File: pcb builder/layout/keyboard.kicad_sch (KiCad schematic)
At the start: 154 parts

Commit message: submoduling all folders KEKW
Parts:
- added U1: Elite-C, symbol keebio:Elite-C
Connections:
- net col0: now also U1.11 (8/PB4)
- net col1: now also U1.12 (9/PB5)
- net col10: now also U1.16 (15/PB1)
- net col11: now also U1.17 (A0/PF7)
- net col12: now also U1.18 (A1/PF6)
- net col13: now also U1.19 (A2/PF5)
- net col14: now also U1.20 (A3/PF4)
- net col2: now also U1.25 (B7)
- net col3: now also U1.26 (D5)
- net col4: now also U1.27 (C7)
- net col5: now also U1.28 (F1)
- net col6: now also U1.29 (F0)
- net col7: now also U1.13 (10/PB6)
- net col8: now also U1.14 (16/PB2)
- net col9: now also U1.15 (14/PB3)
- net row0: now also U1.5 (2/PD1)
- net row1: now also U1.6 (3/PD0)
- net row2: now also U1.7 (4/PD4)
- net row3: now also U1.8 (5/PC6)
- net row4: now also U1.9 (6/PD7)
- net row5: now also U1.10 (7/PE6)
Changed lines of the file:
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@@
+    )
+  )
+  (global_label "row1" (shape input) (at 427.99 54.61 180)
+    (effects (font (size 1.27 1.27)) (justify right))
+    (property "Intersheetrefs" "${INTERSHEET_REFS}" (at 427.99 54.61 0)
+      (effects (font (size 1.27 1.27)) hide)
+    )
+  )
+  (global_label "col4" (shape input) (at 445.77 80.01 270)
+    (effects (font (size 1.27 1.27)) (justify right))
+    (property "Intersheetrefs" "${INTERSHEET_REFS}" (at 445.77 80.01 0)
+      (effects (font (size 1.27 1.27)) hide)
+    )
+  )
+  (global_label "col8" (shape input) (at 463.55 67.31 0)
+    (effects (font (size 1.27 1.27)) (justify left))
+    (property "Intersheetrefs" "${INTERSHEET_REFS}" (at 463.55 67.31 0)
+      (effects (font (size 1.27 1.27)) hide)
     )
   )
@@
     )
   )
+  (global_label "row0" (shape input) (at 427.99 52.07 180)
+    (effects (font (size 1.27 1.27)) (justify right))
+    (property "Intersheetrefs" "${INTERSHEET_REFS}" (at 427.99 52.07 0)
+      (effects (font (size 1.27 1.27)) hide)
+    )
+  )
   (global_label "col13" (shape input) (at 375.92 16.51 180)
     (effects (font (size 1.27 1.27)) (justify right))
@@
     )
   )
+  (global_label "row5" (shape input) (at 427.99 64.77 180)
+    (effects (font (size 1.27 1.27)) (justify right))
+    (property "Intersheetrefs" "${INTERSHEET_REFS}" (at 427.99 64.77 0)
+      (effects (font (size 1.27 1.27)) hide)
+    )
+  )
   (global_label "col6" (shape input) (at 198.12 16.51 180)
     (effects (font (size 1.27 1.27)) (justify right))
@@
     )
   )
+  (global_label "row3" (shape input) (at 427.99 59.69 180)
+    (effects (font (size 1.27 1.27)) (justify right))
+    (property "Intersheetrefs" "${INTERSHEET_REFS}" (at 427.99 59.69 0)
+      (effects (font (size 1.27 1.27)) hide)
+    )
+  )
+  (global_label "col14" (shape input) (at 463.55 52.07 0)
+    (effects (font (size 1.27 1.27)) (justify left))
+    (property "Intersheetrefs" "${INTERSHEET_REFS}" (at 463.55 52.07 0)
+      (effects (font (size 1.27 1.27)) hide)
+    )
+  )
   (global_label "row1" (shape input) (at 22.86 60.96 180)
     (effects (font (size 1.27 1.27)) (justify right))
@@
     )
   )
+  (global_label "col2" (shape input) (at 440.69 80.01 270)
+    (effects (font (size 1.27 1.27)) (justify right))
+    (property "Intersheetrefs" "${INTERSHEET_REFS}" (at 440.69 80.01 0)
+      (effects (font (size 1.27 1.27)) hide)
+    )
+  )
+  (global_label "col5" (shape input) (at 448.31 80.01 270)
+    (effects (font (size 1.27 1.27)) (justify right))
+    (property "Intersheetrefs" "${INTERSHEET_REFS}" (at 448.31 80.01 0)
+      (effects (font (size 1.27 1.27)) hide)
+    )
+  )
   (global_label "col5" (shape input) (at 172.72 16.51 180)
     (effects (font (size 1.27 1.27)) (justify right))
@@
     )
   )
+  (global_label "col10" (shape input) (at 463.55 62.23 0)
+    (effects (font (size 1.27 1.27)) (justify left))
+    (property "Intersheetrefs" "${INTERSHEET_REFS}" (at 463.55 62.23 0)
+      (effects (font (size 1.27 1.27)) hide)
+    )
+  )
+  (global_label "col13" (shape input) (at 463.55 54.61 0)
+    (effects (font (size 1.27 1.27)) (justify left))
+    (property "Intersheetrefs" "${INTERSHEET_REFS}" (at 463.55 54.61 0)
+      (effects (font (size 1.27 1.27)) hide)
+    )
+  )
+  (global_label "col7" (shape input) (at 463.55 69.85 0)
+    (effects (font (size 1.27 1.27)) (justify left))
+    (property "Intersheetrefs" "${INTERSHEET_REFS}" (at 463.55 69.85 0)
+      (effects (font (size 1.27 1.27)) hide)
+    )
+  )
+  (global_label "col11" (shape input) (at 463.55 59.69 0)
+    (effects (font (size 1.27 1.27)) (justify left))
+    (property "Intersheetrefs" "${INTERSHEET_REFS}" (at 463.55 59.69 0)
+      (effects (font (size 1.27 1.27)) hide)
+    )
+  )
+  (global_label "col0" (shape input) (at 427.99 67.31 180)
+    (effects (font (size 1.27 1.27)) (justify right))
+    (property "Intersheetrefs" "${INTERSHEET_REFS}" (at 427.99 67.31 0)
+      (effects (font (size 1.27 1.27)) hide)
+    )
+  )
+  (global_label "row2" (shape input) (at 427.99 57.15 180)
+    (effects (font (size 1.27 1.27)) (justify right))
+    (property "Intersheetrefs" "${INTERSHEET_REFS}" (at 427.99 57.15 0)
+      (effects (font (size 1.27 1.27)) hide)
+    )
+  )
   (global_label "col14" (shape input) (at 401.32 16.51 180)
     (effects (font (size 1.27 1.27)) (justify right))
@@
     )
   )
+  (global_label "row4" (shape input) (at 427.99 62.23 180)
+    (effects (font (size 1.27 1.27)) (justify right))
+    (property "Intersheetrefs" "${INTERSHEET_REFS}" (at 427.99 62.23 0)
+      (effects (font (size 1.27 1.27)) hide)
+    )
+  )
   (global_label "row5" (shape input) (at 22.86 162.56 180)
     (effects (font (size 1.27 1.27)) (justify right))
@@
     )
   )
+  (global_label "col9" (shape input) (at 463.55 64.77 0)
+    (effects (font (size 1.27 1.27)) (justify left))
+    (property "Intersheetrefs" "${INTERSHEET_REFS}" (at 463.55 64.77 0)
+      (effects (font (size 1.27 1.27)) hide)
+    )
+  )
   (global_label "col7" (shape input) (at 223.52 16.51 180)
     (effects (font (size 1.27 1.27)) (justify right))
@@
     )
   )
+  (global_label "col3" (shape input) (at 443.23 80.01 270)
+    (effects (font (size 1.27 1.27)) (justify right))
+    (property "Intersheetrefs" "${INTERSHEET_REFS}" (at 443.23 80.01 0)
+      (effects (font (size 1.27 1.27)) hide)
+    )
+  )
+  (global_label "col12" (shape input) (at 463.55 57.15 0)
+    (effects (font (size 1.27 1.27)) (justify left))
+    (property "Intersheetrefs" "${INTERSHEET_REFS}" (at 463.55 57.15 0)
+      (effects (font (size 1.27 1.27)) hide)
+    )
+  )
+  (global_label "col6" (shape input) (at 450.85 80.01 270)
+    (effects (font (size 1.27 1.27)) (justify right))
+    (property "Intersheetrefs" "${INTERSHEET_REFS}" (at 450.85 80.01 0)
+      (effects (font (size 1.27 1.27)) hide)
+    )
+  )
+  (global_label "col1" (shape input) (at 427.99 69.85 180)
+    (effects (font (size 1.27 1.27)) (justify right))
+    (property "Intersheetrefs" "${INTERSHEET_REFS}" (at 427.99 69.85 0)
+      (effects (font (size 1.27 1.27)) hide)
+    )
+  )
   (symbol (lib_id "Device:D_Small") (at 135.89 83.82 90) (unit 1)
     (in_bom yes) (on_board yes) (dnp no)
@@
         )
       )
+    )
+  )
+  (symbol (lib_id "keebio:Elite-C") (at 445.77 55.88 0) (unit 1)
+    (in_bom yes) (on_board yes) (dnp no) (fields_autoplaced)
+    (property "Reference" "U1" (at 445.77 34.29 0)
+      (effects (font (size 1.524 1.524)))
+    )
+    (property "Value" "Elite-C" (at 445.77 36.83 0)
+      (effects (font (size 1.524 1.524)))
+    )
+    (property "Footprint" "" (at 472.44 119.38 90)
+      (effects (font (size 1.524 1.524)) hide)
+    )
+    (property "Datasheet" "" (at 472.44 119.38 90)
+      (effects (font (size 1.524 1.524)) hide)
+    )
+    (pin "1")
+    (pin "10")
+    (pin "11")
+    (pin "12")
+    (pin "13")
+    (pin "14")
+    (pin "15")
+    (pin "16")
+    (pin "17")
+    (pin "18")
+    (pin "19")
+    (pin "2")
+    (pin "20")
+    (pin "21")
+    (pin "22")
+    (pin "23")
+    (pin "24")
+    (pin "25")
+    (pin "26")
+    (pin "27")
+    (pin "28")
+    (pin "29")
+    (pin "3")
+    (pin "4")
+    (pin "5")
+    (pin "6")
+    (pin "7")
+    (pin "8")
+    (pin "9")
+    (instances
+      (project "keyboard"
+        (path "/218ad51d-6f09-4269-b673-c44cb9c7d5b4"
+          (reference "U1") (unit 1)
+        )
+      )

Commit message: successfully added elite-c
still need to make routes
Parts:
- U1: footprint (none) -> Keebio-Parts:Elite-C
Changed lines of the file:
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@@
       (effects (font (size 1.524 1.524)))
     )
-    (property "Footprint" "" (at 472.44 119.38 90)
+    (property "Footprint" "Keebio-Parts:Elite-C" (at 472.44 119.38 90)
       (effects (font (size 1.524 1.524)) hide)
     )

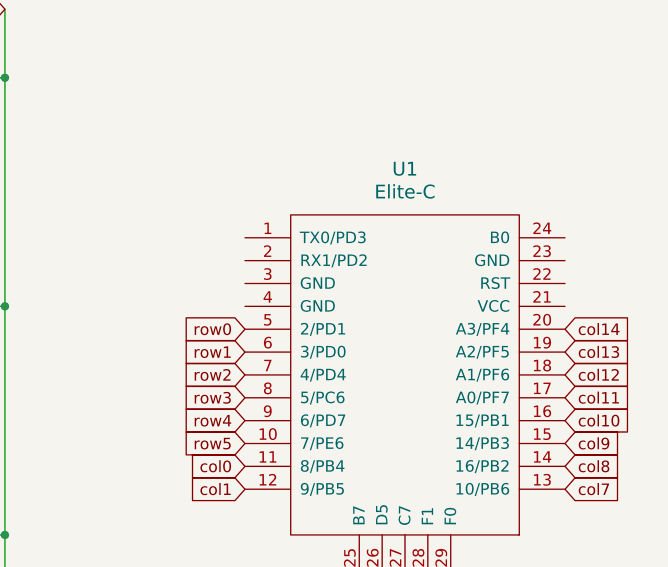
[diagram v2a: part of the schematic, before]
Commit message: traced diodes and switches
Need to reposition elite-c and do traces for rows and cols to elite-c.
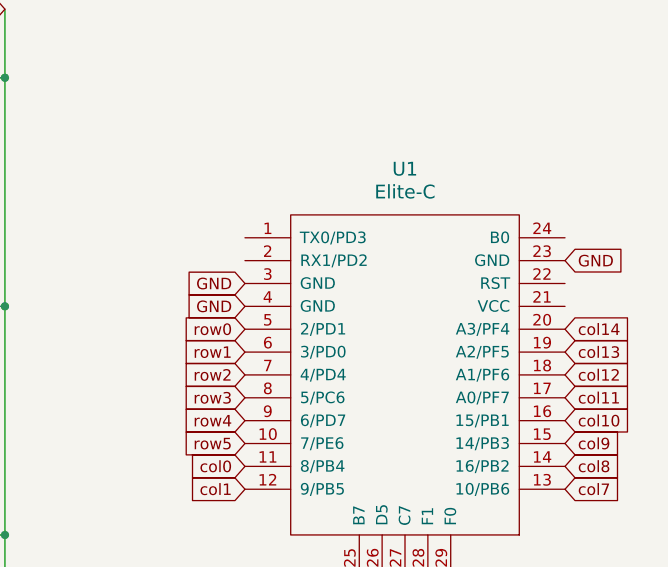
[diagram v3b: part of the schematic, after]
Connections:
- net GND: now reaches U1.23 (GND)
- net GND: now also U1.3 (GND), U1.4 (GND)
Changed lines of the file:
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@@
+    )
+  )
+  (global_label "GND" (shape input) (at 427.99 46.99 180)
+    (effects (font (size 1.27 1.27)) (justify right))
+    (property "Intersheetrefs" "${INTERSHEET_REFS}" (at 427.99 46.99 0)
+      (effects (font (size 1.27 1.27)) hide)
     )
   )
@@
     (effects (font (size 1.27 1.27)) (justify left))
     (property "Intersheetrefs" "${INTERSHEET_REFS}" (at 463.55 52.07 0)
+      (effects (font (size 1.27 1.27)) hide)
+    )
+  )
+  (global_label "GND" (shape input) (at 427.99 49.53 180)
+    (effects (font (size 1.27 1.27)) (justify right))
+    (property "Intersheetrefs" "${INTERSHEET_REFS}" (at 427.99 49.53 0)
       (effects (font (size 1.27 1.27)) hide)
     )
@@
       (effects (font (size 1.27 1.27)) hide)
     )
+  )
+  (global_label "GND" (shape input) (at 463.55 44.45 0)
+    (effects (font (size 1.27 1.27)) (justify left))
+    (property "Intersheetrefs" "${INTERSHEET_REFS}" (at 463.55 44.45 0)
+      (effects (font (size 1.27 1.27)) hide)
+    )

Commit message: retraced everything for promicro.
Thanks Keepo for help. Hope it works now.
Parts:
- removed U1: Elite-C, Keebio-Parts:Elite-C, symbol keebio:Elite-C
- added U2: ProMicro, Keebio-Parts:ArduinoProMicro, symbol keebio:ProMicro
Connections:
- net col10 is gone; now on net col5: K_10.1 (COL), K_25.1 (COL), K_39.1 (COL), K_52.1 (COL), K_66.1 (COL), K_73.1 (COL)
- net col11 is gone; now on net col5: K_11.1 (COL), K_26.1 (COL), K_40.1 (COL), K_53.1 (COL), K_67.1 (COL), K_74.1 (COL)
- net col12 is gone; now on net col6: K_12.1 (COL), K_27.1 (COL), K_41.1 (COL), K_54.1 (COL)
- net col13 is gone; now on net col6: K_13.1 (COL), K_55.1 (COL), K_68.1 (COL), K_75.1 (COL)
- net col14 is gone; now on net col7: K_14.1 (COL), K_28.1 (COL), K_42.1 (COL), K_76.1 (COL)
- net col8 is gone; now on net col4: K_23.1 (COL), K_37.1 (COL), K_50.1 (COL), K_64.1 (COL), K_8.1 (COL)
- net col9 is gone; now on net col4: K_24.1 (COL), K_38.1 (COL), K_51.1 (COL), K_65.1 (COL), K_9.1 (COL)
- net GND: now also U2.23 (GND), U2.3 (GND), U2.4 (GND)
- net col0: now also K_1.1 (COL), K_16.1 (COL), K_30.1 (COL), K_57.1 (COL), K_70.1 (COL), U2.11 (8/PB4)
- net col1: now also K_17.1 (COL), K_18.1 (COL), K_2.1 (COL), K_3.1 (COL), K_31.1 (COL), K_32.1 (COL), K_44.1 (COL), K_45.1 (COL), K_58.1 (COL), K_59.1 (COL), K_71.1 (COL), U2.12 (9/PB5); no longer K_1.1 (COL), K_16.1 (COL), K_30.1 (COL), K_57.1 (COL), K_70.1 (COL)
- net col2: now also K_19.1 (COL), K_20.1 (COL), K_33.1 (COL), K_34.1 (COL), K_4.1 (COL), K_46.1 (COL), K_47.1 (COL), K_5.1 (COL), K_60.1 (COL), K_61.1 (COL), U2.20 (A3/PF4); no longer K_17.1 (COL), K_2.1 (COL), K_31.1 (COL), K_44.1 (COL), K_58.1 (COL)
- net col3: now also K_21.1 (COL), K_22.1 (COL), K_35.1 (COL), K_36.1 (COL), K_48.1 (COL), K_49.1 (COL), K_6.1 (COL), K_62.1 (COL), K_63.1 (COL), K_7.1 (COL), K_72.1 (COL), U2.19 (A2/PF5); no longer K_18.1 (COL), K_3.1 (COL), K_32.1 (COL), K_45.1 (COL), K_59.1 (COL), K_71.1 (COL)
- net col4: now also U2.18 (A1/PF6); no longer K_19.1 (COL), K_33.1 (COL), K_4.1 (COL), K_46.1 (COL), K_60.1 (COL)
- net col5: now also U2.17 (A0/PF7); no longer K_20.1 (COL), K_34.1 (COL), K_47.1 (COL), K_5.1 (COL), K_61.1 (COL)
- net col6: now also U2.15 (14/PB3); no longer K_21.1 (COL), K_35.1 (COL), K_48.1 (COL), K_6.1 (COL), K_62.1 (COL), K_72.1 (COL)
- net col7: now also U2.13 (10/PB6); no longer K_22.1 (COL), K_36.1 (COL), K_49.1 (COL), K_63.1 (COL), K_7.1 (COL)
- net row0: now also U2.5 (2/PD1)
- net row1: now also U2.6 (3/PD0)
- net row2: now also U2.7 (4/PD4)
- net row3: now also U2.8 (5/PC6)
- net row4: now also U2.9 (6/PD7)
- net row5: now also U2.10 (7/PE6)
